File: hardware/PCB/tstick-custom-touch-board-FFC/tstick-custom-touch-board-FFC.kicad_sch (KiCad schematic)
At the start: 20 parts, among them IC1 CY8C206X6A

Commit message: cleaned up the pcb designs for the touch extension boards, created BOM and gerber files for fabrication and assembly
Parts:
- C1: Description Value Pkg (none) -> 2200 pF ±10% 50V Ceramic Capacitor X7R 0603 (1608 Metric); Digikey Part # (none) -> 1276-1990-1-ND; Mfg Part # (none) -> CL10B222KB8NFNC
- C2: Description Value Pkg (none) -> 0.1 µF ±10% 50V Ceramic Capacitor X7R 0603 (1608 Metric); Digikey Part # (none) -> 1276-1000-1-ND; Mfg Part # (none) -> CL10B104KB8NNNC
- I2C1, I2C2, INT1, INT2: Description Value Pkg (none) -> Connector Header Surface Mount, Right Angle 4 position 0.03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; Digikey Part # (none) -> 455-SM04B-SRSS-TBCT-ND; Mfg Part # (none) -> SM04B-SRSS-TB
- IC1: Description Value Pkg (none) -> MCU 8K FLASH 1K SRAM 48QFN; Digikey Part # (none) -> CY8C20636A-24LTXI-ND; Mfg Part # (none) -> CY8C20636A-24LTXI
- R1, R2: Description Value Pkg (none) -> 100 Ohms ±1% 0.25W, 1/4W Chip Resistor 0603 (1608 Metric) A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; Digikey Part # (none) -> 10-ERJ-UP3F1000VCT-ND; Mfg Part # (none) -> ERJ-UP3F1000V
- R3, R4: Description Value Pkg (none) -> 47 kOhms ±0.1% 0.2W, 1/5W Chip Resistor 0603 (1608 Metric) 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; Digikey Part # (none) -> P20162CT-ND; Mfg Part # (none) -> ERJ-PB3B4702V
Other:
- company: (none) -> Input Devices and Musical Interaction Lab, McGill University
- title: (none) -> T-Stick Touch Board
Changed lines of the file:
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@@
 (kicad_sch (version 20230121) (generator eeschema)
   (paper "A4")
+  (title_block
+    (title "T-Stick Touch Board")
+    (date "2023-09")
+    (rev "1")
+    (company "Input Devices and Musical Interaction Lab, McGill University")
+  )
   (junction (at 134.62 119.38) (diameter 0) (color 0 0 0 0)
   )
@@
     )
     (property "Datasheet" "~" (at 228.6 137.16 0)
+      (effects (font (size 1.27 1.27)) hide)
+    )
+    (property "Description Value Pkg" "Connector Header Surface Mount, Right Angle 4 position 0.039\" (1.00mm)" (at 228.6 137.16 0)
+      (effects (font (size 1.27 1.27)) hide)
+    )
+    (property "Mfg Part #" "SM04B-SRSS-TB" (at 228.6 137.16 0)
+      (effects (font (size 1.27 1.27)) hide)
+    )
+    (property "Digikey Part #" "455-SM04B-SRSS-TBCT-ND" (at 228.6 137.16 0)
+      (effects (font (size 1.27 1.27)) hide)
+    )
+    (property "Alternate Part #" "" (at 228.6 137.16 0)
       (effects (font (size 1.27 1.27)) hide)
     )
@@
     )
     (property "Datasheet" "" (at 46.99 76.2 0)
+      (effects (font (size 1.27 1.27)) hide)
+    )
+    (property "Description Value Pkg" "MCU 8K FLASH 1K SRAM 48QFN" (at 46.99 76.2 0)
+      (effects (font (size 1.27 1.27)) hide)
+    )
+    (property "Mfg Part #" "CY8C20636A-24LTXI" (at 46.99 76.2 0)
+      (effects (font (size 1.27 1.27)) hide)
+    )
+    (property "Digikey Part #" "CY8C20636A-24LTXI-ND" (at 46.99 76.2 0)
+      (effects (font (size 1.27 1.27)) hide)
+    )
+    (property "Alternate Part #" "" (at 46.99 76.2 0)
       (effects (font (size 1.27 1.27)) hide)
     )
@@
       (effects (font (size 1.27 1.27)) hide)
     )
+    (property "Description Value Pkg" "0.1 µF ±10% 50V Ceramic Capacitor X7R 0603 (1608 Metric)" (at 21.59 69.85 0)
+      (effects (font (size 1.27 1.27)) hide)
+    )
+    (property "Mfg Part #" "CL10B104KB8NNNC" (at 21.59 69.85 0)
+      (effects (font (size 1.27 1.27)) hide)
+    )
+    (property "Digikey Part #" "1276-1000-1-ND" (at 21.59 69.85 0)
+      (effects (font (size 1.27 1.27)) hide)
+    )
+    (property "Alternate Part #" "" (at 21.59 69.85 0)
+      (effects (font (size 1.27 1.27)) hide)
+    )
     (pin "1")
     (pin "2")
@@
       (effects (font (size 1.27 1.27)) hide)
     )
+    (property "Description Value Pkg" "100 Ohms ±1% 0.25W, 1/4W Chip Resistor 0603 (1608 Metric) Anti-Sulfur, Automotive AEC-Q200, Pulse Withstanding Thick Film" (at 82.55 68.58 0)
+      (effects (font (size 1.27 1.27)) hide)
+    )
+    (property "Mfg Part #" "ERJ-UP3F1000V" (at 82.55 68.58 0)
+      (effects (font (size 1.27 1.27)) hide)
+    )
+    (property "Digikey Part #" "10-ERJ-UP3F1000VCT-ND" (at 82.55 68.58 0)
+      (effects (font (size 1.27 1.27)) hide)
+    )
+    (property "Alternate Part #" "" (at 82.55 68.58 0)
+      (effects (font (size 1.27 1.27)) hide)
+    )
     (pin "1")
     (pin "2")
@@
       (effects (font (size 1.27 1.27)) hide)
     )
+    (property "Description Value Pkg" "47 kOhms ±0.1% 0.2W, 1/5W Chip Resistor 0603 (1608 Metric) Automotive AEC-Q200, Pulse Withstanding Thick Film" (at 264.16 82.55 0)
+      (effects (font (size 1.27 1.27)) hide)
+    )
+    (property "Mfg Part #" "ERJ-PB3B4702V" (at 264.16 82.55 0)
+      (effects (font (size 1.27 1.27)) hide)
+    )
+    (property "Digikey Part #" "P20162CT-ND" (at 264.16 82.55 0)
+      (effects (font (size 1.27 1.27)) hide)
+    )
+    (property "Alternate Part #" "" (at 264.16 82.55 0)
+      (effects (font (size 1.27 1.27)) hide)
+    )
     (pin "1")
     (pin "2")
@@
       (effects (font (size 1.27 1.27)) hide)
     )
+    (property "Description Value Pkg" "100 Ohms ±1% 0.25W, 1/4W Chip Resistor 0603 (1608 Metric) Anti-Sulfur, Automotive AEC-Q200, Pulse Withstanding Thick Film" (at 82.55 66.04 0)
+      (effects (font (size 1.27 1.27)) hide)
+    )
+    (property "Mfg Part #" "ERJ-UP3F1000V" (at 82.55 66.04 0)
+      (effects (font (size 1.27 1.27)) hide)
+    )
+    (property "Digikey Part #" "10-ERJ-UP3F1000VCT-ND" (at 82.55 66.04 0)
+      (effects (font (size 1.27 1.27)) hide)
+    )
+    (property "Alternate Part #" "" (at 82.55 66.04 0)
+      (effects (font (size 1.27 1.27)) hide)
+    )
     (pin "1")
     (pin "2")
@@
     )
     (property "Datasheet" "~" (at 196.85 137.16 0)
+      (effects (font (size 1.27 1.27)) hide)
+    )
+    (property "Description Value Pkg" "Connector Header Surface Mount, Right Angle 4 position 0.039\" (1.00mm)" (at 196.85 137.16 0)
+      (effects (font (size 1.27 1.27)) hide)
+    )
+    (property "Mfg Part #" "SM04B-SRSS-TB" (at 196.85 137.16 0)
+      (effects (font (size 1.27 1.27)) hide)
+    )
+    (property "Digikey Part #" "455-SM04B-SRSS-TBCT-ND" (at 196.85 137.16 0)
+      (effects (font (size 1.27 1.27)) hide)
+    )
+    (property "Alternate Part #" "" (at 196.85 137.16 0)
       (effects (font (size 1.27 1.27)) hide)
     )
@@
       (effects (font (size 1.27 1.27)) hide)
     )
+    (property "Description Value Pkg" "2200 pF ±10% 50V Ceramic Capacitor X7R 0603 (1608 Metric)" (at 69.85 130.81 0)
+      (effects (font (size 1.27 1.27)) hide)
+    )
+    (property "Mfg Part #" "CL10B222KB8NFNC" (at 69.85 130.81 0)
+      (effects (font (size 1.27 1.27)) hide)
+    )
+    (property "Digikey Part #" "1276-1990-1-ND" (at 69.85 130.81 0)
+      (effects (font (size 1.27 1.27)) hide)
+    )
+    (property "Alternate Part #" "" (at 69.85 130.81 0)
+      (effects (font (size 1.27 1.27)) hide)
+    )
     (pin "1")
     (pin "2")
@@
       (effects (font (size 1.27 1.27)) hide)
     )
+    (property "Description Value Pkg" "47 kOhms ±0.1% 0.2W, 1/5W Chip Resistor 0603 (1608 Metric) Automotive AEC-Q200, Pulse Withstanding Thick Film" (at 232.41 82.55 0)
+      (effects (font (size 1.27 1.27)) hide)
+    )
+    (property "Mfg Part #" "ERJ-PB3B4702V" (at 232.41 82.55 0)
+      (effects (font (size 1.27 1.27)) hide)
+    )
+    (property "Digikey Part #" "P20162CT-ND" (at 232.41 82.55 0)
+      (effects (font (size 1.27 1.27)) hide)
+    )
+    (property "Alternate Part #" "" (at 232.41 82.55 0)
+      (effects (font (size 1.27 1.27)) hide)
+    )
     (pin "1")
     (pin "2")
@@
     )
     (property "Datasheet" "~" (at 247.65 29.21 0)
+      (effects (font (size 1.27 1.27)) hide)
+    )
+    (property "Description Value Pkg" "Connector Header Surface Mount, Right Angle 4 position 0.039\" (1.00mm)" (at 247.65 29.21 0)
+      (effects (font (size 1.27 1.27)) hide)
+    )
+    (property "Mfg Part #" "SM04B-SRSS-TB" (at 247.65 29.21 0)
+      (effects (font (size 1.27 1.27)) hide)
+    )
+    (property "Digikey Part #" "455-SM04B-SRSS-TBCT-ND" (at 247.65 29.21 0)
+      (effects (font (size 1.27 1.27)) hide)
+    )
+    (property "Alternate Part #" "" (at 247.65 29.21 0)
       (effects (font (size 1.27 1.27)) hide)
     )
@@
       (effects (font (size 1.27 1.27)) hide)
     )
+    (property "Description Value Pkg" "Connector Header Surface Mount, Right Angle 4 position 0.039\" (1.00mm)" (at 214.63 29.21 0)
+      (effects (font (size 1.27 1.27)) hide)
+    )
+    (property "Mfg Part #" "SM04B-SRSS-TB" (at 214.63 29.21 0)
+      (effects (font (size 1.27 1.27)) hide)
+    )
+    (property "Digikey Part #" "455-SM04B-SRSS-TBCT-ND" (at 214.63 29.21 0)
+      (effects (font (size 1.27 1.27)) hide)
+    )
+    (property "Alternate Part #" "" (at 214.63 29.21 0)
+      (effects (font (size 1.27 1.27)) hide)
+    )

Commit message: removed libaries not related to projects, cleaned up global and project specific libraries, changed capsense controller to smaller 6x6mm package
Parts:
- added J1: Conn_01x01, TestPoint:TestPoint_Pad_D2.0mm, symbol Connector_Generic:Conn_01x01
- FFC1: footprint molex-ffc-connectors:CON_541323262_MOL -> Molex_FFC Connector:CON_541323262_MOL
- I2C1, I2C2, INT1, INT2: footprint Connector_JST:JST_SH_SM04B-SRSS-TB_1x04-1MP_P1.00mm_Horizontal -> JST-footprints:JST_SH_SM04B-SRSS-TB_1x04-1MP_P1.00mm_Horizontal
- IC1: footprint cap-touch-breakout:QFN48-LEADS -> CY8C20646A-CY8C20636A-footprint:QFN-48_EP_6x6_Pitch0.4mm; symbol touch-sensor:CY8C206X6A -> cy8c206x6a:CY8C206X6A; Description Value Pkg MCU 8K FLASH 1K SRAM 48QFN -> IC CAPSENSE 16KB FLASH 48QFN; Digikey Part # CY8C20636A-24LTXI-ND -> 448-CY8C20646A-24LQXI-ND; Mfg Part # CY8C20636A-24LTXI -> CY8C20646A-24LQXI
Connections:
- net RES: now also J1.1 (Pin_1)
- net PR/SCL: now reaches IC1.17 ((PR/SCL)P1[1]), R1.2
- net PR/SDA: now reaches IC1.22 ((PR/SDA)P1[0]), R2.2
- net P01: now reaches C1.1, IC1.48 ((INT)P0[1])
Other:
- note added: "CY8C206xx6A Sensor"
- note added: "RST for Programming"
- note removed: "CY8C260x Sensor"
- moved on the sheet: C2

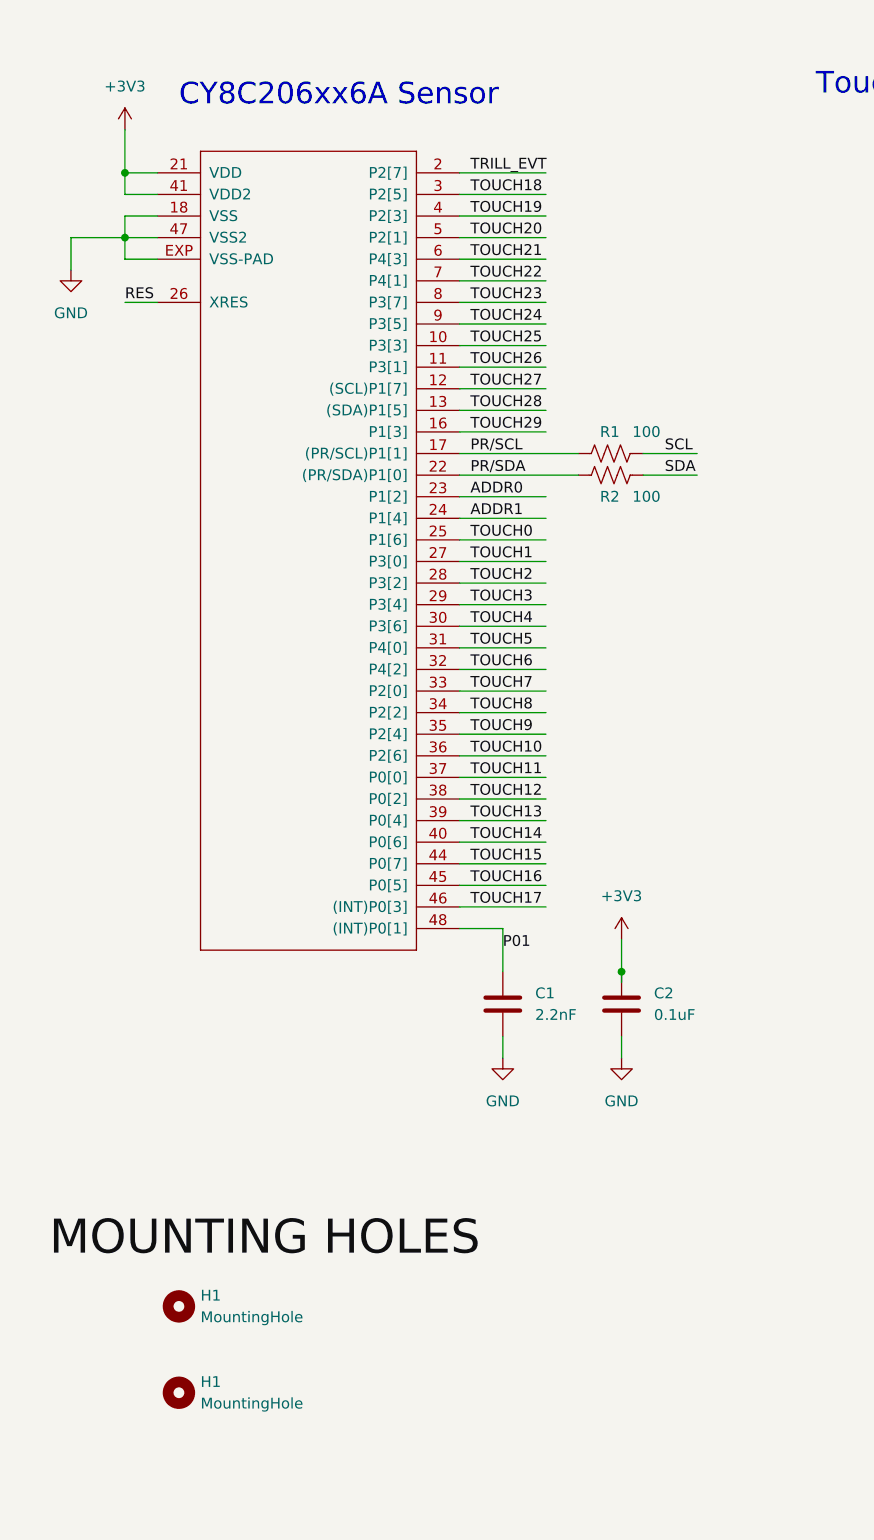
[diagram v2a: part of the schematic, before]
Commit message: removed dropped ideas, re organised datasheets, created project for integrated touch sensor
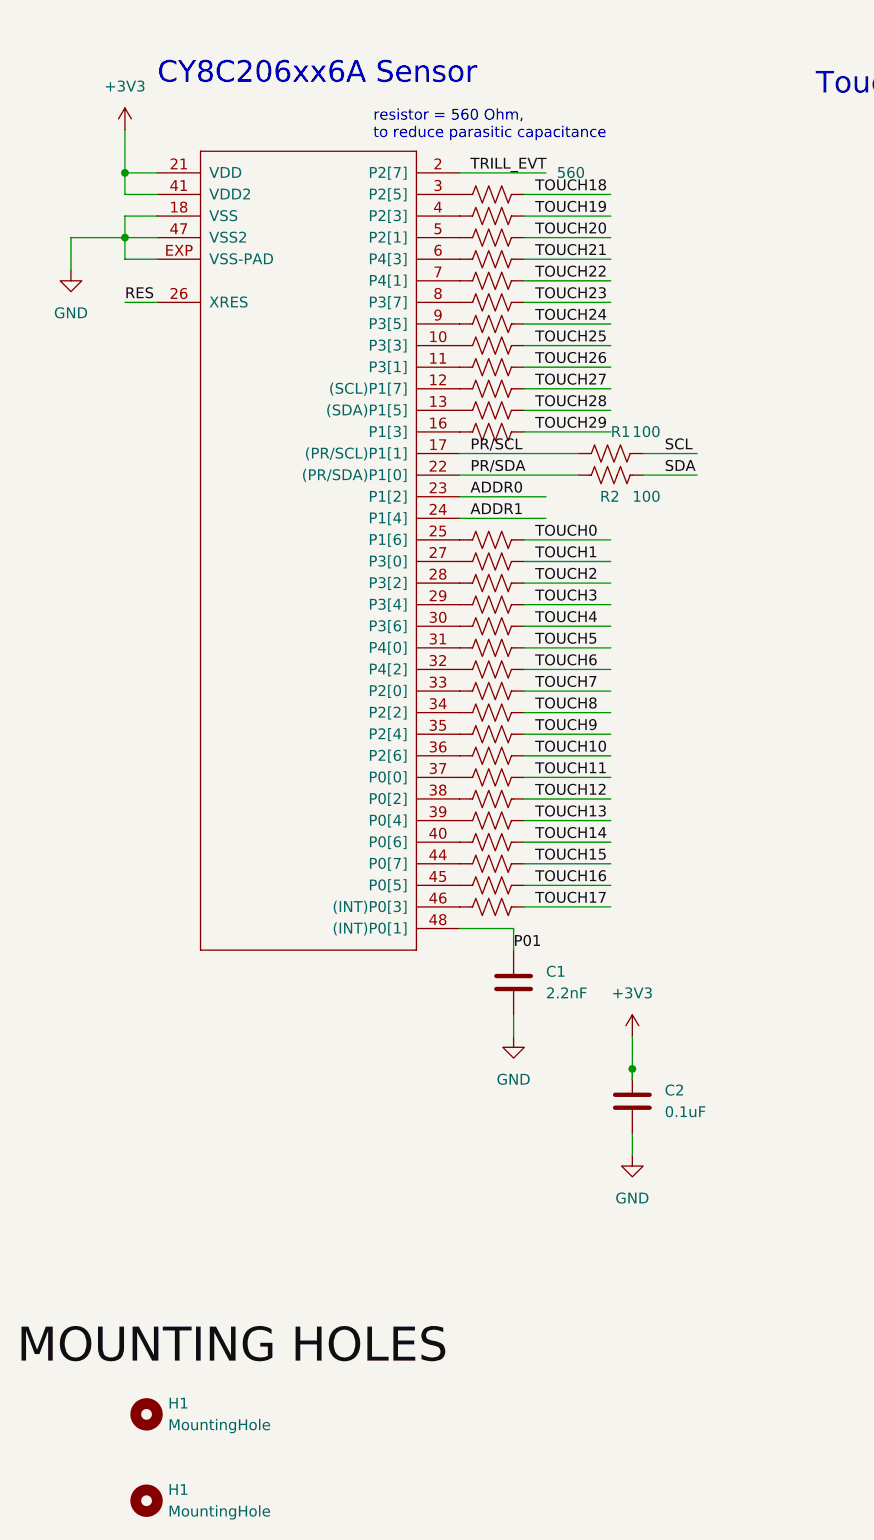
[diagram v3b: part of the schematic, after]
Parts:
- added R10, R11, R12, R13, R14, R15, R16, R17, R18, R19, R20, R21, R22, R23, R24, R25, R26, R27, R28, R29, R30, R31, R32, R33, R34, R5, R6, R7, R8, R9: 560, Resistor_SMD:R_0201_0603Metric, symbol Device:R_US
- C1: footprint Capacitor_SMD:C_0603_1608Metric -> Capacitor_SMD:C_0201_0603Metric; Description Value Pkg 2200 pF ±10% 50V Ceramic Capacitor X7R 0603 (1608 Metric) -> 2200 pF ±10% 10V Ceramic Capacitor X7R 0201 (0603 Metric); Mfg Part # CL10B222KB8NFNC -> CL03B222KP3NNNC
- C2: footprint Capacitor_SMD:C_0603_1608Metric -> Capacitor_SMD:C_0201_0603Metric; Description Value Pkg 0.1 µF ±10% 50V Ceramic Capacitor X7R 0603 (1608 Metric) -> 0.1 µF ±10% 6.3V Ceramic Capacitor X5R 0201 (0603 Metric); Digikey Part # 1276-1000-1-ND -> 1276-1013-1-ND; Mfg Part # CL10B104KB8NNNC -> CL03A104KQ3NNNC
- R1, R2: footprint Resistor_SMD:R_0603_1608Metric -> Resistor_SMD:R_0201_0603Metric; Description Value Pkg 100 Ohms ±1% 0.25W, 1/4W Chip Resistor 0603 (1608 Metric) A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 -> 100 Ohms ±1% 0.05W, 1/20W Chip Resistor 0201 (0603 Metric) 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; Digikey Part # 10-ERJ-UP3F1000VCT-ND -> P122654CT-ND; Mfg Part # ERJ-UP3F1000V -> ERJ-1GNF1000C
- R3, R4: footprint Resistor_SMD:R_0603_1608Metric -> Resistor_SMD:R_0201_0603Metric; Description Value Pkg 47 kOhms ±0.1% 0.2W, 1/5W Chip Resistor 0603 (1608 Metric) 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 -> 47 kOhms ±1% 0.05W, 1/20W Chip Resistor 0201 (0603 Metric) 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; Digikey Part # P20162CT-ND -> P123032CT-ND; Mfg Part # ERJ-PB3B4702V -> ERJ-1GNF4702C
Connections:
- net TOUCH0: now also R17.1; no longer IC1.25 (P1[6])
- net TOUCH1: now also R18.1; no longer IC1.27 (P3[0])
- net TOUCH10: now also R27.1; no longer IC1.36 (P2[6])
- net TOUCH11: now also R28.1; no longer IC1.37 (P0[0])
- net TOUCH12: now also R29.1; no longer IC1.38 (P0[2])
- net TOUCH13: now also R30.1; no longer IC1.39 (P0[4])
- net TOUCH14: now also R31.1; no longer IC1.40 (P0[6])
- net TOUCH15: now also R32.1; no longer IC1.44 (P0[7])
- net TOUCH16: now also R33.1; no longer IC1.45 (P0[5])
- net TOUCH17: now also R34.1; no longer IC1.46 ((INT)P0[3])
- net TOUCH18: now also R5.1; no longer IC1.3 (P2[5])
- net TOUCH19: now also R6.1; no longer IC1.4 (P2[3])
- net TOUCH2: now also R19.1; no longer IC1.28 (P3[2])
- net TOUCH20: now also R7.1; no longer IC1.5 (P2[1])
- net TOUCH21: now also R8.1; no longer IC1.6 (P4[3])
- net TOUCH22: now also R9.1; no longer IC1.7 (P4[1])
- net TOUCH23: now also R10.1; no longer IC1.8 (P3[7])
- net TOUCH24: now also R11.1; no longer IC1.9 (P3[5])
- net TOUCH25: now also R12.1; no longer IC1.10 (P3[3])
- net TOUCH26: now also R13.1; no longer IC1.11 (P3[1])
- net TOUCH27: now also R14.1; no longer IC1.12 ((SCL)P1[7])
- net TOUCH28: now also R15.1; no longer IC1.13 ((SDA)P1[5])
- net TOUCH29: now also R16.1; no longer IC1.16 (P1[3])
- net TOUCH3: now also R20.1; no longer IC1.29 (P3[4])
- net TOUCH4: now also R21.1; no longer IC1.30 (P3[6])
- net TOUCH5: now also R22.1; no longer IC1.31 (P4[0])
- net TOUCH6: now also R23.1; no longer IC1.32 (P4[2])
- net TOUCH7: now also R24.1; no longer IC1.33 (P2[0])
- net TOUCH8: now also R25.1; no longer IC1.34 (P2[2])
- net TOUCH9: now also R26.1; no longer IC1.35 (P2[4])
- new net: IC1.6 (P4[3]), R8.2
- new net: IC1.10 (P3[3]), R12.2
- new net: IC1.11 (P3[1]), R13.2
- new net: IC1.12 ((SCL)P1[7]), R14.2
- new net: IC1.13 ((SDA)P1[5]), R15.2
- new net: IC1.16 (P1[3]), R16.2
- new net: IC1.25 (P1[6]), R17.2
- new net: IC1.27 (P3[0]), R18.2
- new net: IC1.28 (P3[2]), R19.2
- new net: IC1.29 (P3[4]), R20.2
- new net: IC1.3 (P2[5]), R5.2
- new net: IC1.30 (P3[6]), R21.2
- new net: IC1.31 (P4[0]), R22.2
- new net: IC1.32 (P4[2]), R23.2
- new net: IC1.33 (P2[0]), R24.2
- new net: IC1.34 (P2[2]), R25.2
- new net: IC1.35 (P2[4]), R26.2
- new net: IC1.36 (P2[6]), R27.2
- new net: IC1.37 (P0[0]), R28.2
- new net: IC1.38 (P0[2]), R29.2
- new net: IC1.39 (P0[4]), R30.2
- new net: IC1.4 (P2[3]), R6.2
- new net: IC1.40 (P0[6]), R31.2
- new net: IC1.44 (P0[7]), R32.2
- new net: IC1.45 (P0[5]), R33.2
- new net: IC1.46 ((INT)P0[3]), R34.2
- new net: IC1.5 (P2[1]), R7.2
- new net: IC1.7 (P4[1]), R9.2
- new net: IC1.8 (P3[7]), R10.2
- new net: IC1.9 (P3[5]), R11.2
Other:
- note added: "resistor = 560 Ohm, to reduce parasitic capacitance"
- moved on the sheet: C1, C2, H1
